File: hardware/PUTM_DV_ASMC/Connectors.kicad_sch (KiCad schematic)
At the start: 7 parts, among them J1 FTSH-107-01-L-D-K, J2 IPBS-110-01-T-D-GP

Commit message: done schematic v1
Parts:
- removed J2: IPBS-110-01-T-D-GP, IPBS11001TDGP, symbol IPBS-110-01-T-D-GP:IPBS-110-01-T-D-GP
- added H1: MountingHole_Pad_MP, MountingHole:MountingHole_4.3mm_M4_DIN965_Pad_TopOnly, symbol Mechanical:MountingHole_Pad_MP
- added J2: IPBS-110-01-XX-D-GP, PDM:IPBT110H1TDRAGP, symbol PDM:IPBS-110-01-T-D-GP
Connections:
- net CAN1+: now also J2.1
- net CAN1-: now also J2.2
- net CAN2+: now also J2.11
- net CAN2-: now also J2.12
- net GND: now also J2.20
- new net ADC: J2.10
- new net ASSI_DI: J2.5
- new net ASSI_DO: J2.4
- new net AS_SAFETY: J2.7
- new net GPIO: J2.19
- new net OUTPUT_ODRIVE: H1.MP
- new net OUT_ASSI: J2.15, J2.16
- new net OUT_BUZZER: J2.3
- new net OUT_EBS: J2.17
- new net OUT_LIDAR: J2.13, J2.14
- new net OUT_RES: J2.18
- new net RES_SAFETY: J2.6
- new net RES_SAFETY_IN: J2.9
- new net RES_SAFETY_OUTPUT: J2.8
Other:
- note added: "MAIN CONNECTOR"
- note added: "ODRIVE OUTPUT"
- moved on the sheet: D13, D14, D15, D16, D17, J1

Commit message: schematic without error
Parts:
- J1: footprint Samacsys:FTSH-107-XX-YYY-D-K -> FTSH-107-XX-YYY-D-K:FTSH-107-XX-YYY-D-K
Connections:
- net OUTPUT_ODRIVE renamed ODRIVE_1
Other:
- moved on the sheet: H1

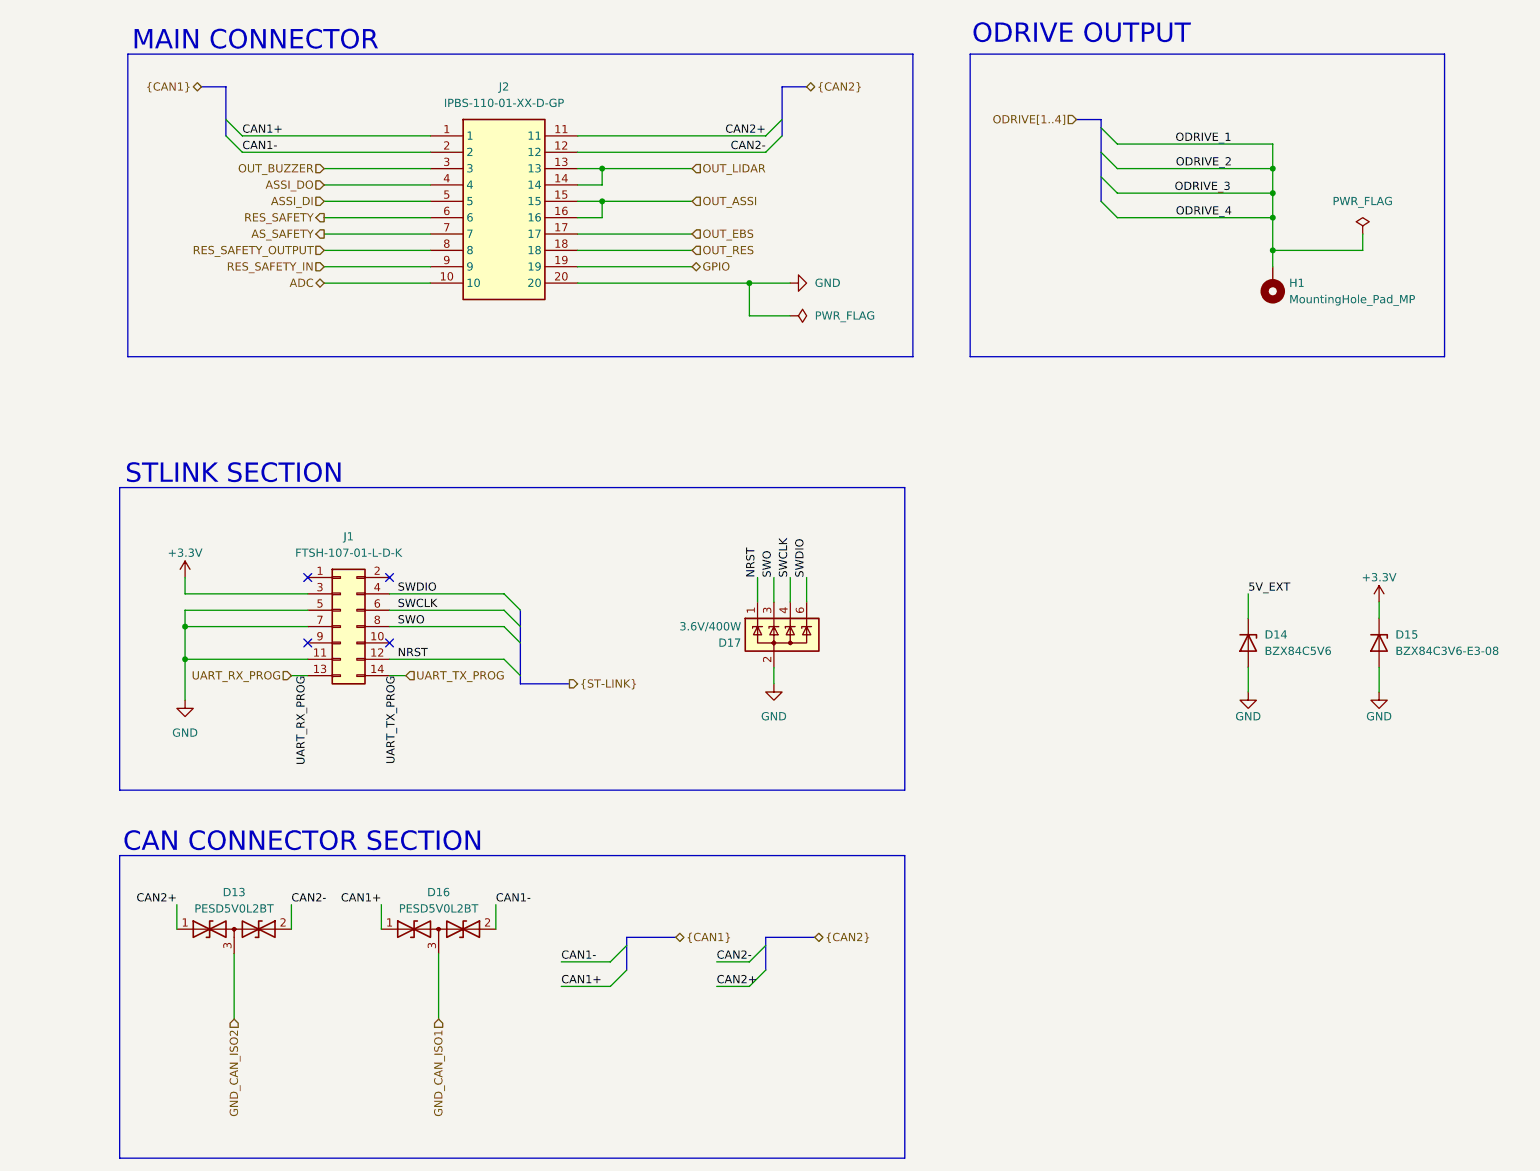
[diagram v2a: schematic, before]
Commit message: tylko dwa bledy z can - schemat na wykonczeniu
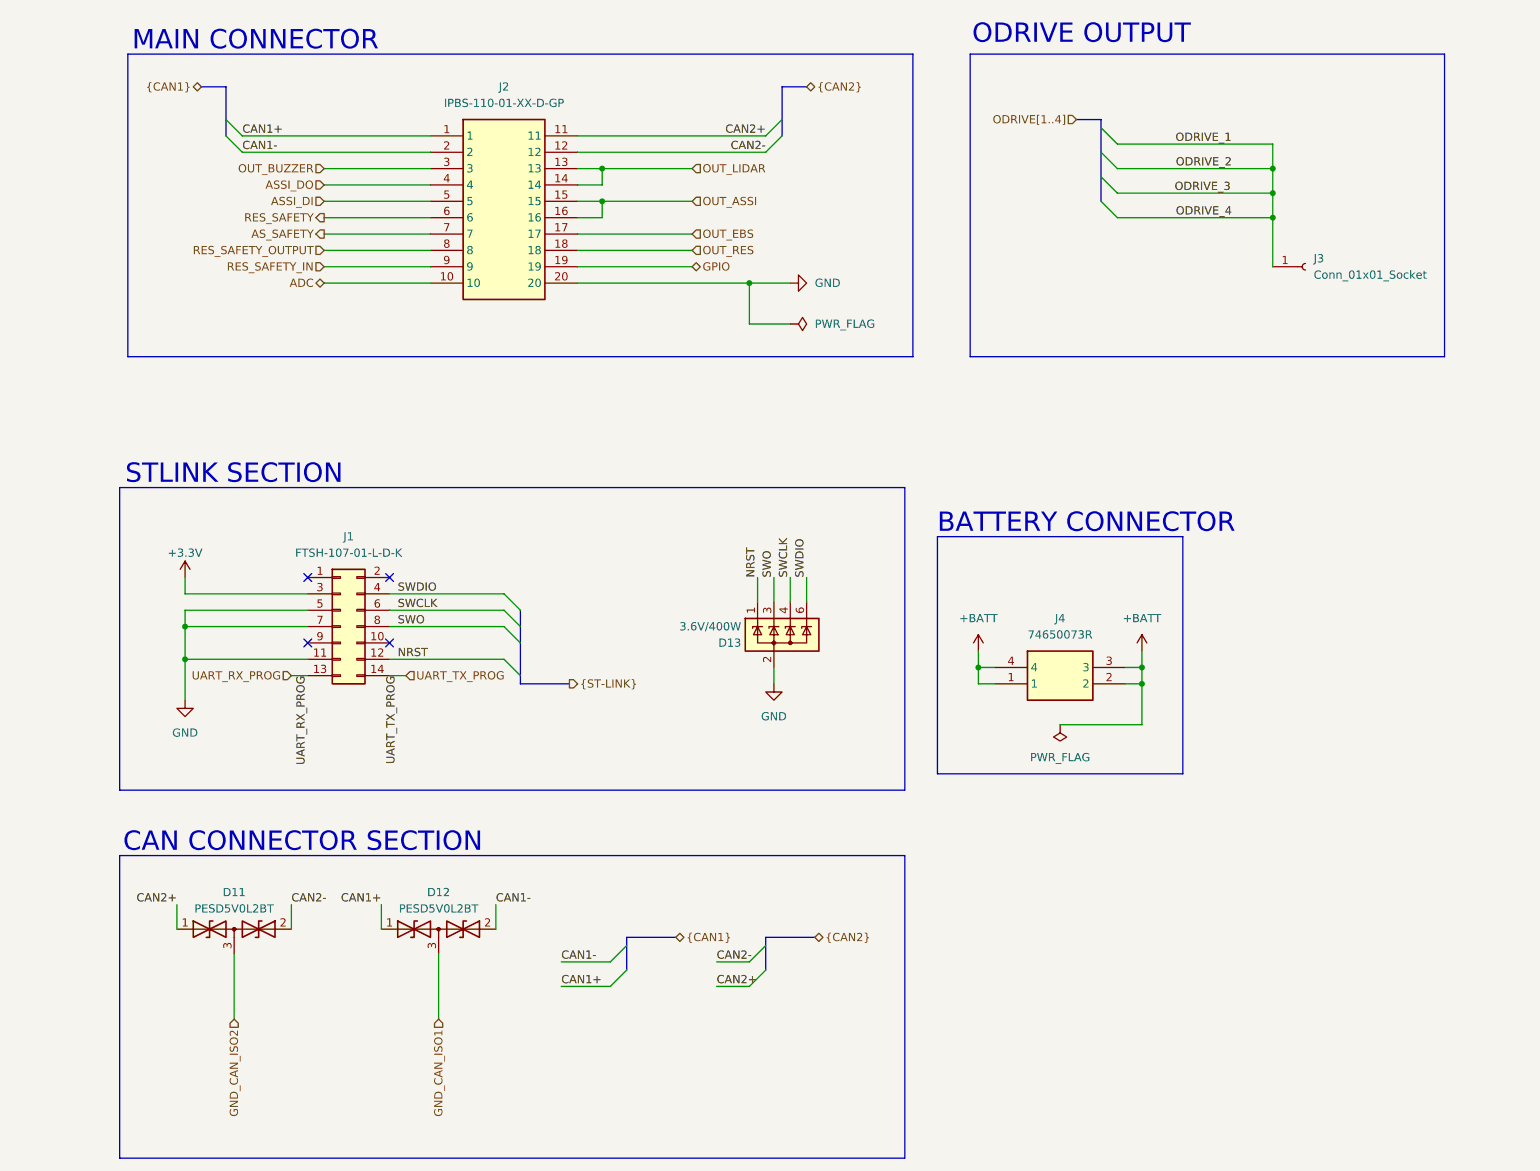
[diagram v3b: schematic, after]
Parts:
- removed D14: BZX84C5V6, Package_TO_SOT_SMD:SOT-23, symbol Diode:BZX84Cxx
- removed D15: BZX84C3V6-E3-08, Package_TO_SOT_SMD:SOT-23, symbol Diode:BZX84Cxx
- removed H1: MountingHole_Pad_MP, MountingHole:MountingHole_4.3mm_M4_DIN965_Pad_TopOnly, symbol Mechanical:MountingHole_Pad_MP
- added J3: Conn_01x01_Socket, Connector_PinHeader_1.00mm:PinHeader_1x01_P1.00mm_Vertical, symbol Connector:Conn_01x01_Socket
- added J4: 74650073R, PDM:74650073R, symbol PDM:74650073R
- renumbered D13 to D11, D16 to D12, D17 to D13
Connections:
- net ODRIVE_1: now also J3.1 (Pin_1)
- new net +BATT: J4.1, J4.2, J4.3, J4.4
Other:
- note added: "BATTERY CONNECTOR"

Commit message: poprawki footprint
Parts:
- J2: footprint PDM:IPBT110H1TDRAGP -> IPBS-110-01-T-D-GP:IPBS11001TDGP
- J4: footprint PDM:74650073R -> 74650073R:74650073R
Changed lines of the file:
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@@
 			)
 		)
-		(property "Footprint" "PDM:IPBT110H1TDRAGP"
+		(property "Footprint" "IPBS-110-01-T-D-GP:IPBS11001TDGP"
 			(at 99.06 130.48 0)
 			(hide yes)
@@
 			)
 		)
-		(property "Footprint" "PDM:74650073R"
+		(property "Footprint" "74650073R:74650073R"
 			(at 184.15 213.03 0)
 			(hide yes)

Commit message: work on power layout
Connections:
- net CAN1+: now also J2.20; no longer J2.1
- net CAN1-: now also J2.19; no longer J2.2
- net CAN2+: now also J2.17; no longer J2.11
- net CAN2-: now also J2.18; no longer J2.12
- net GND: now also J2.1; no longer J2.20
- net GPIO: now also J2.2; no longer J2.19
- net OUT_ASSI: now also J2.13, J2.14; no longer J2.15, J2.16
- net OUT_EBS: now also J2.16; no longer J2.17
- net OUT_LIDAR: now also J2.11, J2.12; no longer J2.13, J2.14
- net OUT_RES: now also J2.15; no longer J2.18

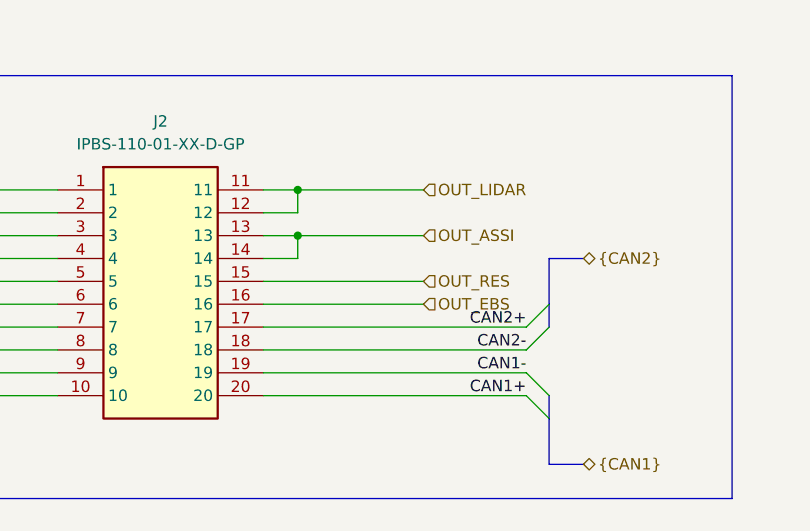
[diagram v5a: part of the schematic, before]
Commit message: make function section
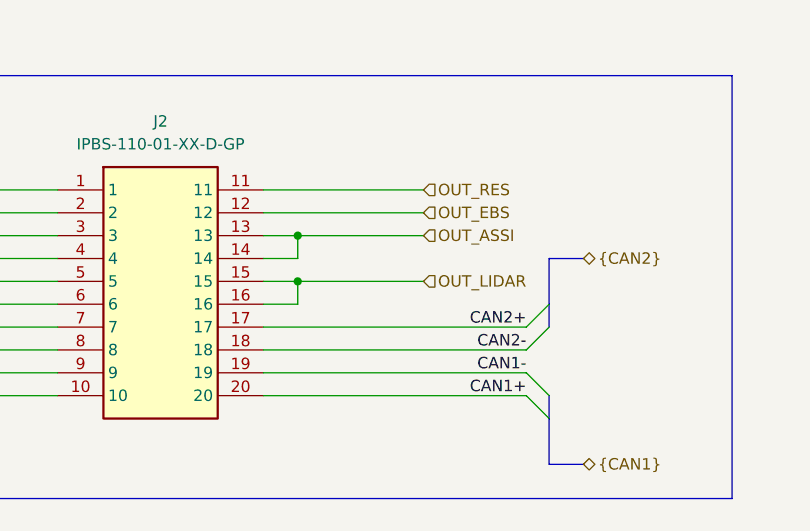
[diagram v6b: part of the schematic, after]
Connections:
- net OUT_EBS: now also J2.12; no longer J2.16
- net OUT_LIDAR: now also J2.15, J2.16; no longer J2.11, J2.12
- net OUT_RES: now also J2.11; no longer J2.15
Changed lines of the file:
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@@
+	)
+	(junction
+		(at 106.68 45.72)
+		(diameter 0)
+		(color 0 0 0 0)
 	)
 	(junction
@@
 	)
 	(junction
-		(at 106.68 35.56)
-		(diameter 0)
-		(color 0 0 0 0)
-	)
-	(junction
 		(at 210.82 48.26)
 		(diameter 0)
@@
 	(wire
 		(pts
-			(xy 106.68 35.56) (xy 120.65 35.56)
-		)
-		(stroke
-			(width 0)
-			(type default)
-		)
-	)
-	(wire
-		(pts
 			(xy 58.42 119.38) (xy 60.96 119.38)
 		)
@@
 	(wire
 		(pts
+			(xy 102.87 45.72) (xy 106.68 45.72)
+		)
+		(stroke
+			(width 0)
+			(type default)
+		)
+	)
+	(wire
+		(pts
 			(xy 130.81 104.14) (xy 130.81 107.95)
 		)
@@
 	(wire
 		(pts
-			(xy 106.68 38.1) (xy 106.68 35.56)
-		)
-		(stroke
-			(width 0)
-			(type default)
-		)
-	)
-	(wire
-		(pts
 			(xy 177.8 127) (xy 190.5 127)
 		)
@@
 	(wire
 		(pts
+			(xy 102.87 38.1) (xy 120.65 38.1)
+		)
+		(stroke
+			(width 0)
+			(type default)
+		)
+	)
+	(wire
+		(pts
 			(xy 73.66 116.84) (xy 91.44 116.84)
 		)
@@
 	(wire
 		(pts
-			(xy 102.87 38.1) (xy 106.68 38.1)
-		)
-		(stroke
-			(width 0)
-			(type default)
-		)
-	)
-	(wire
-		(pts
 			(xy 102.87 40.64) (xy 106.68 40.64)
 		)
@@
 	(wire
 		(pts
-			(xy 102.87 45.72) (xy 120.65 45.72)
+			(xy 102.87 48.26) (xy 106.68 48.26)
+		)
+		(stroke
+			(width 0)
+			(type default)
+		)
+	)
+	(wire
+		(pts
+			(xy 106.68 45.72) (xy 120.65 45.72)
 		)
 		(stroke
@@
 	(wire
 		(pts
-			(xy 102.87 48.26) (xy 120.65 48.26)
-		)
-		(stroke
-			(width 0)
-			(type default)
-		)
-	)
-	(wire
-		(pts
 			(xy 69.85 35.56) (xy 63.5 35.56)
 		)
@@
 		)
 	)
+	(wire
+		(pts
+			(xy 102.87 35.56) (xy 120.65 35.56)
+		)
+		(stroke
+			(width 0)
+			(type default)
+		)
+	)
 	(bus
 		(pts
@@
 		)
 	)
+	(wire
+		(pts
+			(xy 106.68 48.26) (xy 106.68 45.72)
+		)
+		(stroke
+			(width 0)
+			(type default)
+		)
+	)
 	(bus
 		(pts
@@
 		(pts
 			(xy 72.39 154.94) (xy 72.39 158.75)
-		)
-		(stroke
-			(width 0)
-			(type default)
-		)
-	)
-	(wire
-		(pts
-			(xy 102.87 35.56) (xy 106.68 35.56)
 		)
 		(stroke
@@
 		)
 	)
-	(hierarchical_label "OUT_EBS"
-		(shape input)
-		(at 120.65 48.26 0)
-		(effects
-			(font
-				(size 1.27 1.27)
-			)
-			(justify left)
-		)
-	)
 	(hierarchical_label "AS_SAFETY"
 		(shape output)
@@
 		)
 	)
+	(hierarchical_label "OUT_LIDAR"
+		(shape input)
+		(at 120.65 45.72 0)
+		(effects
+			(font
+				(size 1.27 1.27)
+			)
+			(justify left)
+		)
+	)
 	(hierarchical_label "ASSI_DI"
 		(shape input)
@@
 		)
 	)
+	(hierarchical_label "OUT_RES"
+		(shape input)
+		(at 120.65 35.56 0)
+		(effects
+			(font
+				(size 1.27 1.27)
+			)
+			(justify left)
+		)
+	)
+	(hierarchical_label "OUT_EBS"
+		(shape input)
+		(at 120.65 38.1 0)
+		(effects
+			(font
+				(size 1.27 1.27)
+			)
+			(justify left)
+		)
+	)
 	(hierarchical_label "RES_SAFETY"
 		(shape output)
@@
 		)
 	)
-	(hierarchical_label "OUT_RES"
-		(shape input)
-		(at 120.65 45.72 0)
-		(effects
-			(font
-				(size 1.27 1.27)
-			)
-			(justify left)
-		)
-	)
 	(hierarchical_label "GND_CAN_ISO1"
 		(shape input)
@@
 		)
 	)
-	(hierarchical_label "OUT_LIDAR"
-		(shape input)
-		(at 120.65 35.56 0)
-		(effects
-			(font
-				(size 1.27 1.27)
-			)
-			(justify left)
-		)
-	)

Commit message: make zones
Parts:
- removed J3: Conn_01x01_Socket, Connector_PinHeader_1.00mm:PinHeader_1x01_P1.00mm_Vertical, symbol Connector:Conn_01x01_Socket
- added J5: 74650073R, 74650073R:74650073R, symbol PDM:74650073R
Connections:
- net ODRIVE_1: now also J5.2
- new net ODRIVE_2: J5.3
- new net ODRIVE_3: J5.4
- new net ODRIVE_4: J5.1

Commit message: work on supply and zones
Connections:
- net ODRIVE_2 is gone; now on net ODRIVE1: J5.3
- net ODRIVE_3 is gone; now on net ODRIVE1: J5.4
- net ODRIVE_4 is gone; now on net ODRIVE1: J5.1
- net ODRIVE_1 renamed ODRIVE1
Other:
- moved on the sheet: J5
